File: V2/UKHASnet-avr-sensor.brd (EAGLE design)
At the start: 49.5 x 49.2 mm, 32 parts, among them J1 AVR_SPI_PRG_62X3_LOCK, U1 MCP1700-3302E/TO, U2 ATMEGA328P-PU, X1 SMA-142-0711-881/886, Y1 RESONATORPTH

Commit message: Correct cap calue.
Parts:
- C1: value 6.8UF -> 47UF
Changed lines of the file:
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@@
 <attribute name="VALUE" x="19.304" y="9.779" size="0.8128" layer="21" font="vector" ratio="15"/>
 </element>
-<element name="C1" library="1000ufCap" package="CAPPR150-400X1200" value="6.8UF" x="27.94" y="6.35" smashed="yes" rot="R90">
+<element name="C1" library="1000ufCap" package="CAPPR150-400X1200" value="47UF" x="27.94" y="6.35" smashed="yes" rot="R90">
 <attribute name="OC_NEWARK" value="17T5110 " x="27.94" y="6.35" size="1.778" layer="27" rot="R90" display="off"/>
 <attribute name="TOLERANCE" value="±20 %" x="27.94" y="6.35" size="1.778" layer="27" rot="R90" display="off"/>

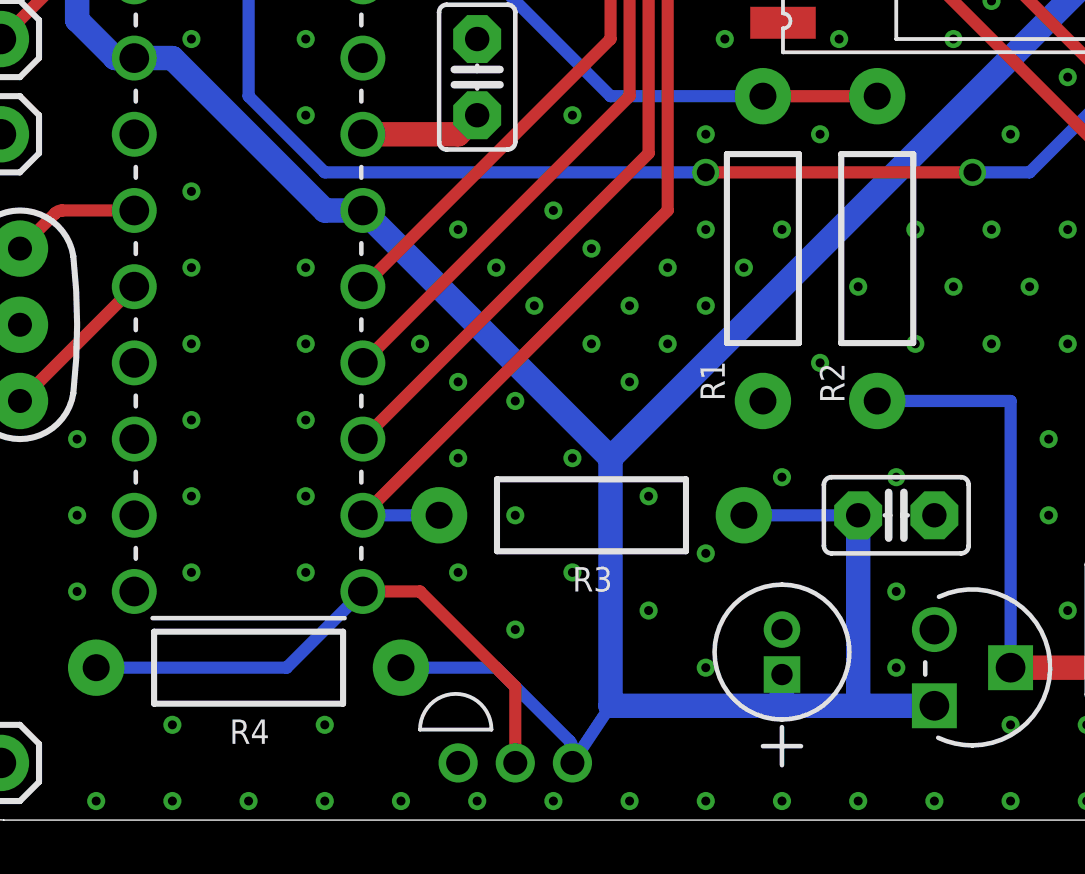
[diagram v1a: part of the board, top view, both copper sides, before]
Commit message: Add resistor values.
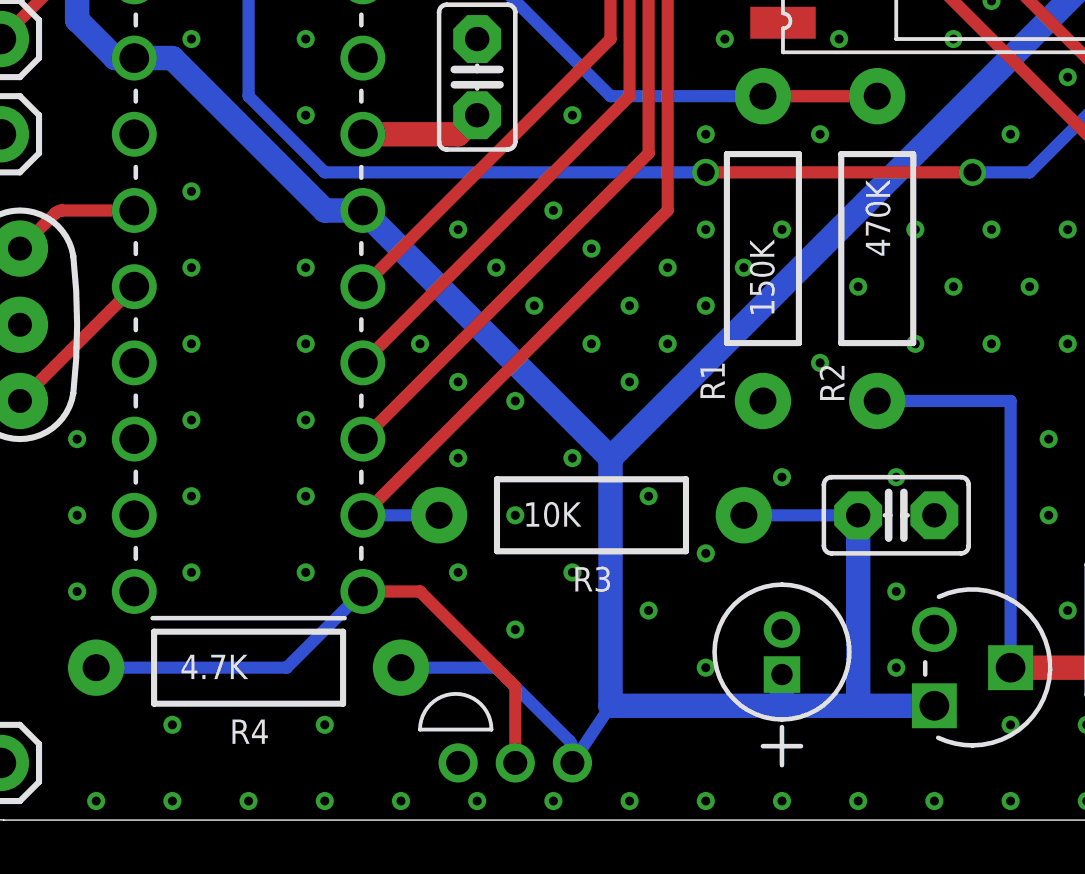
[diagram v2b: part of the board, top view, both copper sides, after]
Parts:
- R1: value (none) -> 150K
- R2: value (none) -> 470K
- R3: value (none) -> 10K
- R4: value (none) -> 4.7K
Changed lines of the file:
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@@
 </element>
 <element name="JP9" library="SparkFun-Connectors" package="1X01" value="M01PTH" x="24.765" y="46.355" smashed="yes"/>
-<element name="R1" library="SparkFun" package="AXIAL-0.4" value="" x="27.305" y="19.05" smashed="yes" rot="R90">
+<element name="R1" library="SparkFun" package="AXIAL-0.4" value="150K" x="27.305" y="19.05" smashed="yes" rot="R90">
 <attribute name="NAME" x="26.035" y="13.97" size="0.8128" layer="25" font="vector" ratio="15" rot="R90"/>
 <attribute name="VALUE" x="27.686" y="16.764" size="0.8128" layer="21" font="vector" ratio="15" rot="R90"/>
 </element>
-<element name="R2" library="SparkFun" package="AXIAL-0.4" value="" x="31.115" y="19.05" smashed="yes" rot="R270">
+<element name="R2" library="SparkFun" package="AXIAL-0.4" value="470K" x="31.115" y="19.05" smashed="yes" rot="R270">
 <attribute name="NAME" x="29.21" y="15.24" size="0.8128" layer="25" font="vector" ratio="15" rot="R270"/>
 <attribute name="VALUE" x="30.734" y="21.336" size="0.8128" layer="21" font="vector" ratio="15" rot="R270"/>
 </element>
-<element name="R3" library="SparkFun" package="AXIAL-0.4" value="" x="21.59" y="10.16" smashed="yes">
+<element name="R3" library="SparkFun" package="AXIAL-0.4" value="10K" x="21.59" y="10.16" smashed="yes">
 <attribute name="NAME" x="20.955" y="7.62" size="0.8128" layer="25" font="vector" ratio="15"/>
 <attribute name="VALUE" x="19.304" y="9.779" size="0.8128" layer="21" font="vector" ratio="15"/>
@@
 <attribute name="OC_FARNELL" value="1848468 " x="27.94" y="6.35" size="1.778" layer="27" rot="R90" display="off"/>
 </element>
-<element name="R4" library="SparkFun" package="AXIAL-0.4" value="" x="10.16" y="5.08" smashed="yes">
+<element name="R4" library="SparkFun" package="AXIAL-0.4" value="4.7K" x="10.16" y="5.08" smashed="yes">
 <attribute name="NAME" x="9.525" y="2.54" size="0.8128" layer="25" font="vector" ratio="15"/>
 <attribute name="VALUE" x="7.874" y="4.699" size="0.8128" layer="21" font="vector" ratio="15"/>
